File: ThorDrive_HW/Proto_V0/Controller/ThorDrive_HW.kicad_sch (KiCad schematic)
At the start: 56 parts, among them J1 Conn_01x04_Socket, J10 Conn_01x03_Socket, J13 CTRL, J2 Conn_01x06_Socket, J3 Conn_01x03_Socket, J4 Conn_01x08_Socket, J5 Conn_01x08_Pin, J6 Conn_01x04_Pin, J7 Conn_01x06_Pin, J8 Conn_01x04_Pin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

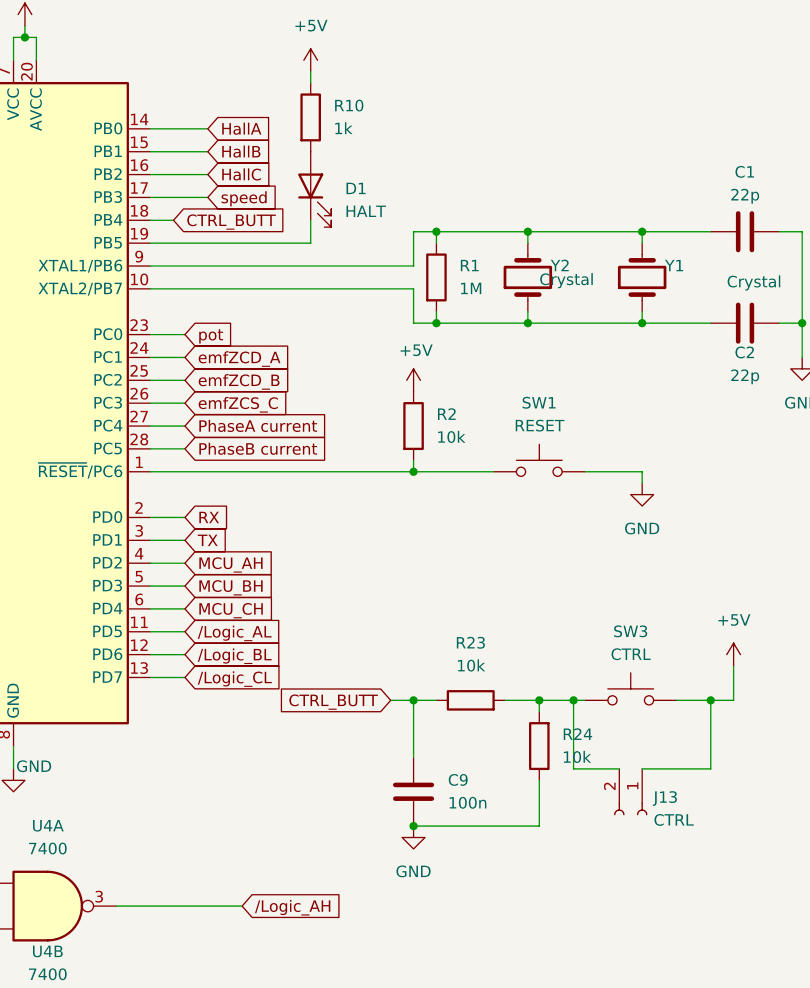
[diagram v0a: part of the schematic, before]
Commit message: Added Basic Drivers, Initialized system manager
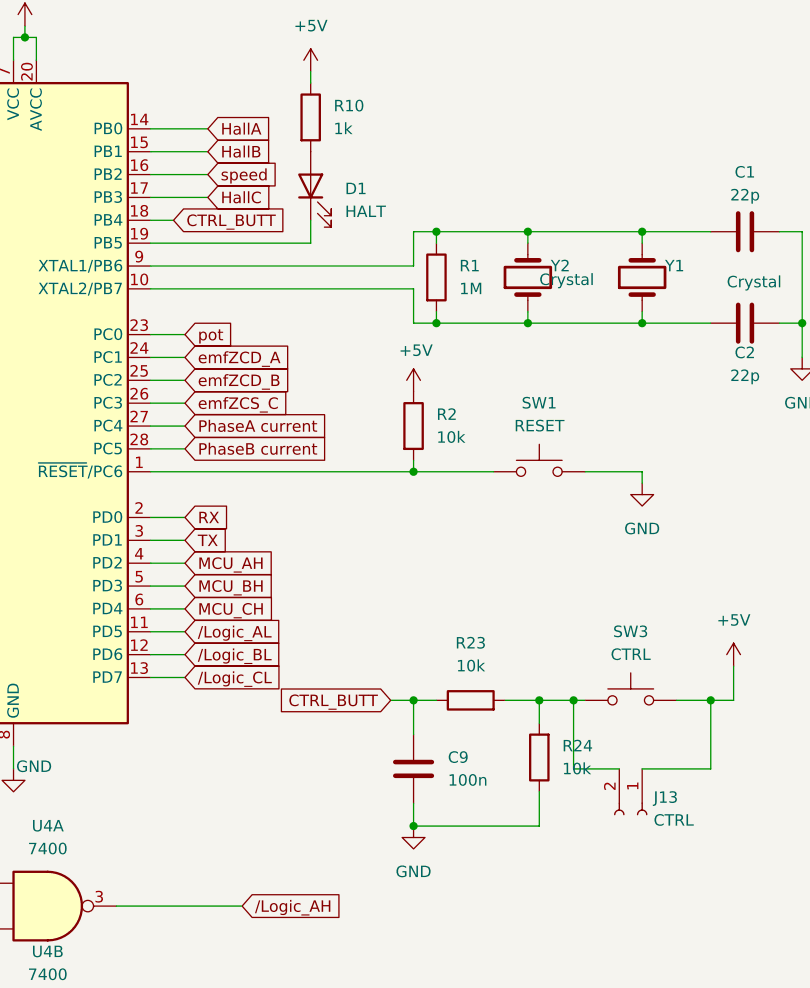
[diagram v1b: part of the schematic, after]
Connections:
- net HallC: now also U1.17 (PB3); no longer U1.16 (PB2)
- net speed: now also U1.16 (PB2); no longer U1.17 (PB3)
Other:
- moved on the sheet: C9, R24
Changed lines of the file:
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@@
 	(wire
 		(pts
-			(xy 93.98 92.71) (xy 93.98 99.06)
+			(xy 93.98 92.71) (xy 93.98 96.52)
 		)
 		(stroke
@@
 	(wire
 		(pts
-			(xy 107.95 93.98) (xy 107.95 92.71)
+			(xy 107.95 95.25) (xy 107.95 92.71)
 		)
 		(stroke
@@
 	(wire
 		(pts
+			(xy 93.98 104.14) (xy 93.98 106.68)
+		)
+		(stroke
+			(width 0)
+			(type default)
+		)
+	)
+	(wire
+		(pts
 			(xy 156.21 125.73) (xy 156.21 128.27)
 		)
@@
 	(wire
 		(pts
-			(xy 107.95 101.6) (xy 107.95 106.68)
+			(xy 107.95 102.87) (xy 107.95 106.68)
 		)
 		(stroke
@@
 		)
 	)
+	(global_label "HallC"
+		(shape input)
+		(at 71.12 36.83 0)
+		(fields_autoplaced yes)
+		(effects
+			(font
+				(size 1.27 1.27)
+			)
+			(justify left)
+		)
+		(property "Intersheetrefs" "${INTERSHEET_REFS}"
+			(at 79.1851 36.83 0)
+			(effects
+				(font
+					(size 1.27 1.27)
+				)
+				(justify left)
+				(hide yes)
+			)
+		)
+	)
 	(global_label "emfZCD_B"
 		(shape input)
@@
 		)
 	)
-	(global_label "speed"
-		(shape input)
-		(at 71.12 36.83 0)
-		(fields_autoplaced yes)
-		(effects
-			(font
-				(size 1.27 1.27)
-			)
-			(justify left)
-		)
-		(property "Intersheetrefs" "${INTERSHEET_REFS}"
-			(at 79.6085 36.83 0)
-			(effects
-				(font
-					(size 1.27 1.27)
-				)
-				(justify left)
-				(hide yes)
-			)
-		)
-	)
 	(global_label "{slash}Logic_CH"
 		(shape input)
@@
 		)
 	)
+	(global_label "speed"
+		(shape input)
+		(at 71.12 34.29 0)
+		(fields_autoplaced yes)
+		(effects
+			(font
+				(size 1.27 1.27)
+			)
+			(justify left)
+		)
+		(property "Intersheetrefs" "${INTERSHEET_REFS}"
+			(at 79.6085 34.29 0)
+			(effects
+				(font
+					(size 1.27 1.27)
+				)
+				(justify left)
+				(hide yes)
+			)
+		)
+	)
 	(global_label "HallB"
 		(shape input)
@@
 		)
 	)
-	(global_label "HallC"
-		(shape input)
-		(at 71.12 34.29 0)
-		(fields_autoplaced yes)
-		(effects
-			(font
-				(size 1.27 1.27)
-			)
-			(justify left)
-		)
-		(property "Intersheetrefs" "${INTERSHEET_REFS}"
-			(at 79.1851 34.29 0)
-			(effects
-				(font
-					(size 1.27 1.27)
-				)
-				(justify left)
-				(hide yes)
-			)
-		)
-	)
 	(global_label "{slash}Logic_BH"
 		(shape input)
@@
 	(symbol
 		(lib_id "Device:C")
-		(at 93.98 102.87 0)
+		(at 93.98 100.33 0)
 		(unit 1)
 		(exclude_from_sim no)
@@
 		(fields_autoplaced yes)
 		(property "Reference" "C9"
-			(at 97.79 101.5999 0)
+			(at 97.79 99.0599 0)
 			(effects
 				(font
@@
 		)
 		(property "Value" "100n"
-			(at 97.79 104.1399 0)
+			(at 97.79 101.5999 0)
 			(effects
 				(font
@@
 		)
 		(property "Footprint" "Capacitor_SMD:C_0805_2012Metric_Pad1.18x1.45mm_HandSolder"
-			(at 94.9452 106.68 0)
+			(at 94.9452 104.14 0)
 			(effects
 				(font
@@
 		)
 		(property "Datasheet" "~"
-			(at 93.98 102.87 0)
+			(at 93.98 100.33 0)
 			(effects
 				(font
@@
 		)
 		(property "Description" "Unpolarized capacitor"
-			(at 93.98 102.87 0)
+			(at 93.98 100.33 0)
 			(effects
 				(font
@@
 	(symbol
 		(lib_id "Device:R")
-		(at 107.95 97.79 180)
+		(at 107.95 99.06 180)
 		(unit 1)
 		(exclude_from_sim no)
@@
 		(fields_autoplaced yes)
 		(property "Reference" "R24"
-			(at 110.49 96.5199 0)
+			(at 110.49 97.7899 0)
 			(effects
 				(font
@@
 		)
 		(property "Value" "10k"
-			(at 110.49 99.0599 0)
+			(at 110.49 100.3299 0)
 			(effects
 				(font
@@
 		)
 		(property "Footprint" "Resistor_SMD:R_1206_3216Metric_Pad1.30x1.75mm_HandSolder"
-			(at 109.728 97.79 90)
+			(at 109.728 99.06 90)
 			(effects
 				(font
@@
 		)
 		(property "Datasheet" "~"
-			(at 107.95 97.79 0)
+			(at 107.95 99.06 0)
 			(effects
 				(font
@@
 		)
 		(property "Description" "Resistor"
-			(at 107.95 97.79 0)
+			(at 107.95 99.06 0)
 			(effects
 				(font
